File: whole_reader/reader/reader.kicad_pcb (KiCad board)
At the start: 2 copper layers, 50 x 58.5 mm, 65 parts, among them U1 LM386, U2 STM32F103C8T6, U3 MCP16301Hx-xCH, U4 MAX3232, Y1 16MHz

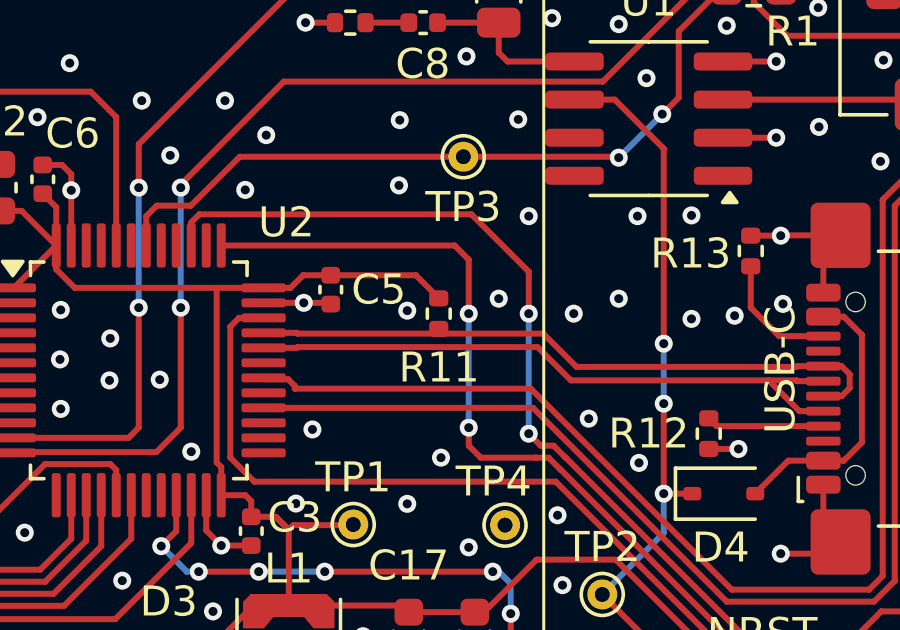
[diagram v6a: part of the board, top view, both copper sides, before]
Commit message: Úprava schémy
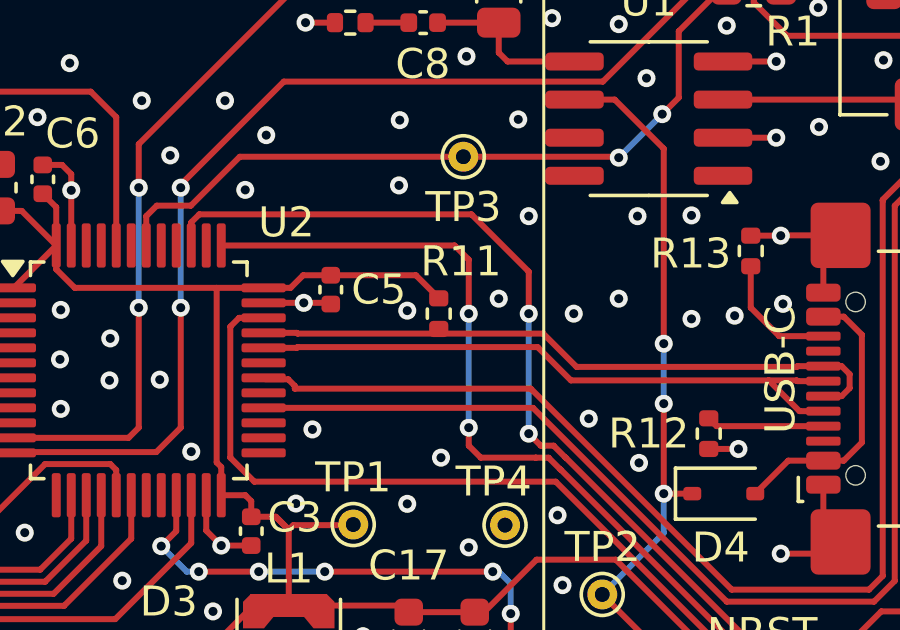
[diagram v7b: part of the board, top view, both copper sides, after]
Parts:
- turned R11 to 90 degrees
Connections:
- R11 pad 1: +3.3V -> USB_D+
- R11 pad 2: USB_D+ -> +3.3V
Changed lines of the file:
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@@
 	(footprint "Resistor_SMD:R_0402_1005Metric"
 		(layer "F.Cu")
-		(at 162 46 -90)
+		(at 162 46 90)
 		(descr "Resistor SMD 0402 (1005 Metric), square (rectangular) end terminal, IPC_7351 nominal, (Body size source: IPC-SM-782 page 72, https://www.pcb-3d.com/wordpress/wp-content/uploads/ipc-sm-782a_amendment_1_and_2.pdf), generated with kicad-footprint-generator")
 		(tags "resistor")
 		(property "Reference" "R11"
-			(at 1.8 -0.01 180)
+			(at 1.74 0.74 0)
 			(layer "F.SilkS")
 			(effects
@@
 		)
 		(property "Datasheet" ""
-			(at 0 0 270)
+			(at 0 0 90)
 			(unlocked yes)
 			(layer "F.Fab")
@@
 		)
 		(property "Description" "Resistor"
-			(at 0 0 270)
+			(at 0 0 90)
 			(unlocked yes)
 			(layer "F.Fab")
@@
 		)
 		(property "Note" ""
-			(at 0 0 270)
+			(at 0 0 90)
 			(unlocked yes)
 			(layer "F.Fab")
@@
 		(attr smd)
 		(fp_line
+			(start -0.153641 -0.38)
+			(end 0.153641 -0.38)
+			(stroke
+				(width 0.12)
+				(type solid)
+			)
+			(layer "F.SilkS")
+		)
+		(fp_line
 			(start -0.153641 0.38)
 			(end 0.153641 0.38)
@@
 		)
 		(fp_line
-			(start -0.153641 -0.38)
-			(end 0.153641 -0.38)
+			(start 0.93 -0.47)
+			(end 0.93 0.47)
 			(stroke
-				(width 0.12)
+				(width 0.05)
 				(type solid)
 			)
-			(layer "F.SilkS")
+			(layer "F.CrtYd")
 		)
 		(fp_line
-			(start -0.93 0.47)
-			(end -0.93 -0.47)
+			(start -0.93 -0.47)
+			(end 0.93 -0.47)
 			(stroke
 				(width 0.05)
@@
 		)
 		(fp_line
-			(start -0.93 -0.47)
-			(end 0.93 -0.47)
+			(start -0.93 0.47)
+			(end -0.93 -0.47)
 			(stroke
 				(width 0.05)
@@
 		)
 		(fp_line
-			(start 0.93 -0.47)
-			(end 0.93 0.47)
+			(start 0.525 -0.27)
+			(end 0.525 0.27)
 			(stroke
-				(width 0.05)
+				(width 0.1)
 				(type solid)
 			)
-			(layer "F.CrtYd")
+			(layer "F.Fab")
 		)
 		(fp_line
-			(start -0.525 0.27)
-			(end -0.525 -0.27)
+			(start -0.525 -0.27)
+			(end 0.525 -0.27)
 			(stroke
 				(width 0.1)
@@
 		)
 		(fp_line
-			(start -0.525 -0.27)
-			(end 0.525 -0.27)
-			(stroke
-				(width 0.1)
-				(type solid)
-			)
-			(layer "F.Fab")
-		)
-		(fp_line
-			(start 0.525 -0.27)
-			(end 0.525 0.27)
+			(start -0.525 0.27)
+			(end -0.525 -0.27)
 			(stroke
 				(width 0.1)
@@
 		)
 		(pad "1" smd roundrect
-			(at -0.51 0 270)
+			(at -0.51 0 90)
+			(size 0.54 0.64)
+			(layers "F.Cu" "F.Mask" "F.Paste")
+			(roundrect_rratio 0.25)
+			(net 25 "USB_D+")
+			(pintype "passive")
+		)
+		(pad "2" smd roundrect
+			(at 0.51 0 90)
 			(size 0.54 0.64)
 			(layers "F.Cu" "F.Mask" "F.Paste")
@@
 			(pintype "passive")
 		)
-		(pad "2" smd roundrect
-			(at 0.51 0 270)
-			(size 0.54 0.64)
-			(layers "F.Cu" "F.Mask" "F.Paste")
-			(roundrect_rratio 0.25)
-			(net 25 "USB_D+")
-			(pintype "passive")
-		)

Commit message: Add jumper for audio
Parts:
- added JP1: SolderJumper_2_Bridged, Jumper:SolderJumper-2_P1.3mm_Bridged_RoundedPad1.0x1.5mm, F.Cu at (159.4, 40.8)
- moved TP3 0.06 mm to (162.8, 40.8)
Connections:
- R1 pad 1: AUDIO_OUT -> Net-(JP1-B)
- TP3 pad 1: AUDIO_OUT -> Net-(JP1-B)
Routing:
- net AUDIO_OUT: track 24.8 -> 8.11 mm, vias 2 -> 0
- net Net-(JP1-B): track 0.00 -> 15.4 mm, vias 0 -> 2
